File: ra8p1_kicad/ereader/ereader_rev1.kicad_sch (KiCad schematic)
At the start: 0 parts

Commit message: Integrate Pcam camera and reserve dual-camera MCU routes (#821)
Join CSI and camera control hierarchy, migrate the radio bus and volume-up input, and preserve the reviewed net partitions. Enlarge root and MCU pages and refresh the 13-page PDF and native BOM.

Record dual-camera lighting and wet-port requirements plus parallel-module qualification gaps. Native/CLI ERC: 121 errors and 2 warnings; full design remains incomplete. Independent connectivity review passed; version and whitespace checks passed. ASCII check retains the pre-existing 63-character PARTS-CHECKLIST failure. Hardware-only hook bypass authorized by the owner.
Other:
- added sheet Pcam 5C camera (camera.kicad_sch)
- sheet RA8P1 IO allocation ports: added CAM_CLK_N, CAM_CLK_P, CAM_D0_N, CAM_D0_P, CAM_D1_N, CAM_D1_P, CAM_PWR_REQ, CAM_SCL, CAM_SDA; removed none

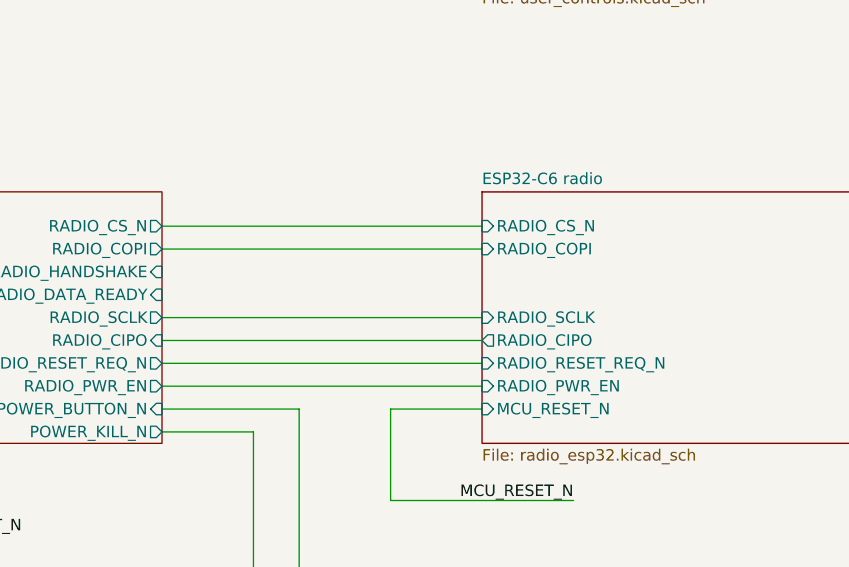
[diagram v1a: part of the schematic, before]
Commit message: hardware: isolate radio handshake outputs through TXU0102
Connect U25 status channels to the RA8P1 hierarchy, add host pulldowns and bypass capacitors, and update conditional OE/load calculations. Refresh sourced native BOM and full schematic PDF. Independent circuit review passed; 117 ERC errors remain in the incomplete design. Refs #821 #846.
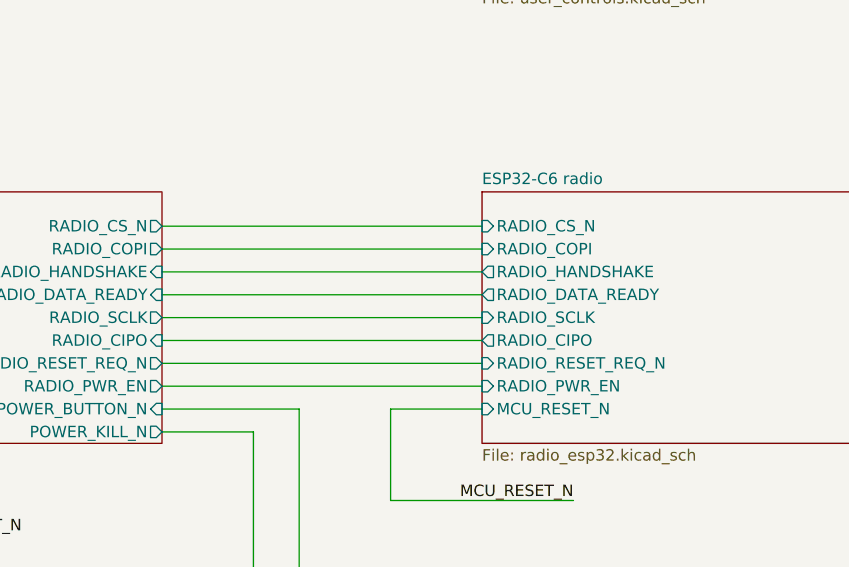
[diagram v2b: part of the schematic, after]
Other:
- sheet ESP32-C6 radio ports: added RADIO_DATA_READY, RADIO_HANDSHAKE; removed none
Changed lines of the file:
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@@
+	(wire
+		(pts
+			(xy 167.64 92.71) (xy 203.2 92.71)
+		)
+		(stroke
+			(width 0)
+			(type default)
+		)
+	)
 	(wire
 		(pts
@@
 		(pts
 			(xy 429.26 134.62) (xy 441.96 134.62)
+		)
+		(stroke
+			(width 0)
+			(type default)
+		)
+	)
+	(wire
+		(pts
+			(xy 167.64 90.17) (xy 203.2 90.17)
 		)
 		(stroke
@@
 			(effects
 				(font
+					(size 1.27 1.27)
+				)
+				(justify left)
+			)
+		)
+		(pin "RADIO_DATA_READY" output
+			(at 203.2 92.71 180)
+			(effects
+				(font
+					(size 1.27 1.27)
+				)
+				(justify left)
+			)
+		)
+		(pin "RADIO_HANDSHAKE" output
+			(at 203.2 90.17 180)
+			(effects
+				(font

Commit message: wip(hardware): preserve schematic cleanup and CEU host ports
Checkpoint cosmetic cleanup across the schematic hierarchy and eleven parallel-camera host ports. Refresh the complete 13-page PDF. All 334 existing net partitions and 271 component records match the prior CEU checkpoint; all 128 ERC identities remain unchanged. Electrical design is incomplete; this is a WIP checkpoint for #821 and #841.
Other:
- sheet RA8P1 IO allocation ports: added CEU_D0, CEU_D1, CEU_D2, CEU_D3, CEU_D4, CEU_D5, CEU_D6, CEU_D7, CEU_HREF, CEU_PCLK, CEU_VSYNC; removed none
